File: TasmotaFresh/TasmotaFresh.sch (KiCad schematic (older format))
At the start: 0 parts

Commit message: initial schematic work
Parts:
- added D1, D2, D3: LED, symbol Device:LED
- added J1: ESP-01S, symbol Connector_Generic:Conn_02x04_Counter_Clockwise
- added J2: FAN, symbol Connector_Generic:Conn_01x04
- added Q1: HIGH, Package_TO_SOT_THT:TO-220-3_Vertical, symbol Triac_Thyristor:TIC226
- added Q2: MEDIUM, Package_TO_SOT_THT:TO-220-3_Vertical, symbol Triac_Thyristor:TIC226
- added Q3: LOW, Package_TO_SOT_THT:TO-220-3_Vertical, symbol Triac_Thyristor:TIC226
- added R1, R2, R3, R4: R, symbol Device:R
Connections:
- new net: J2.1 (Pin_1), Q1.1 (A1)
- new net: Q1.3 (G), R1.1
- new net: J2.2 (Pin_2), Q2.1 (A1)
- new net: Q2.3 (G), R2.1
- new net: J2.3 (Pin_3), Q3.1 (A1)
- new net: Q3.3 (G), R3.2
- new net: D1.1 (K), D2.1 (K), D3.1 (K), R4.1
- new net 3V3: J1.4 (Pin_4)
- new net CH_PD-EN: J1.2 (Pin_2)
- new net GND: J1.1 (Pin_1), J1.8 (Pin_8), R4.2
- new net GPIO0: D2.2 (A), J1.6 (Pin_6), R2.2
- new net GPIO2: D1.2 (A), J1.7 (Pin_7), R1.2
- new net GPIO3: D3.2 (A), J1.5 (Pin_5), R3.1
- new net LINE: Q1.2 (A2), Q2.2 (A2), Q3.2 (A2)
- new net NEUT: J2.4 (Pin_4)
- new net RST: J1.3 (Pin_3)

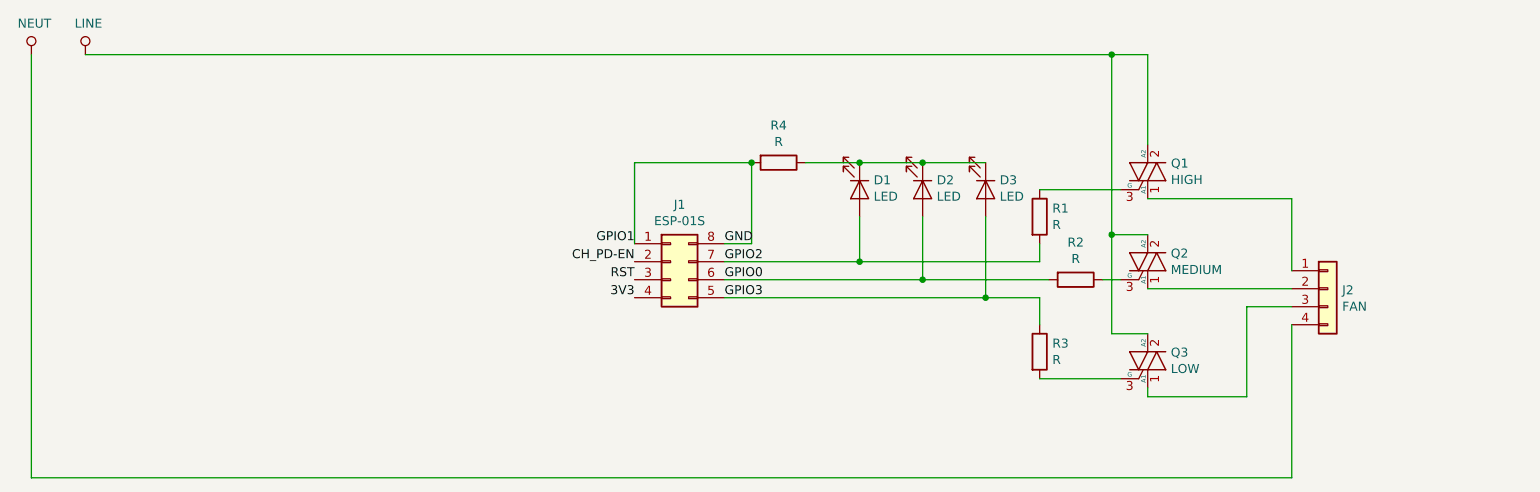
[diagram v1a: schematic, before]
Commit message: updated schematic with power supply section
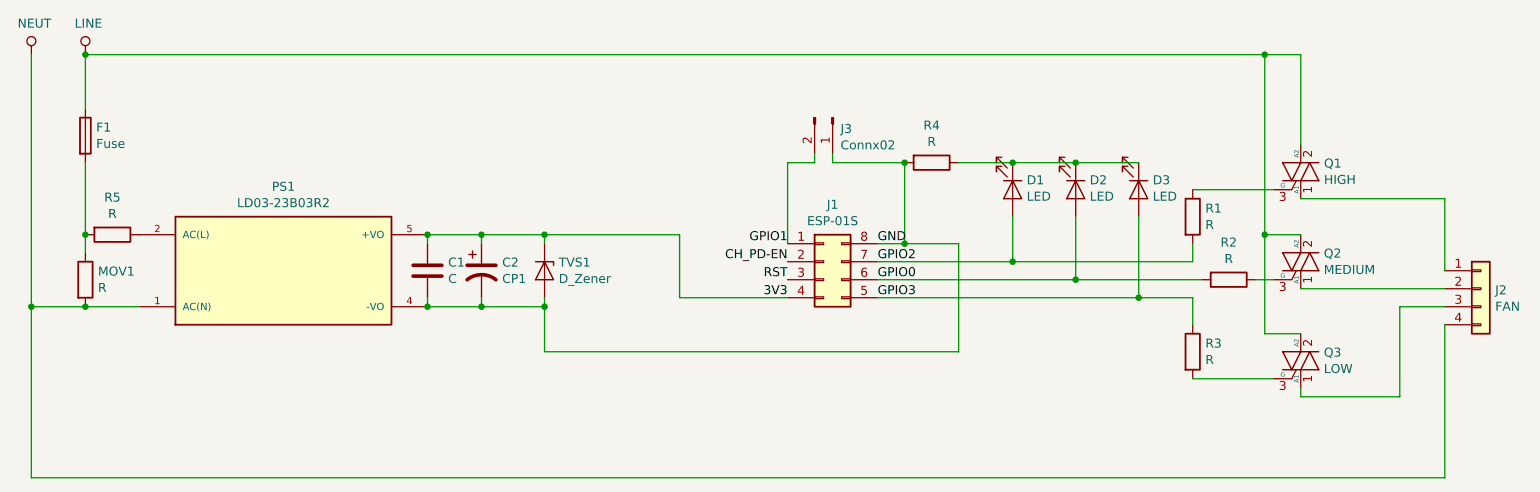
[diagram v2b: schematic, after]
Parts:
- added C1: C, symbol Device:C
- added C2: CP1, symbol Device:CP1
- added F1: Fuse, symbol Device:Fuse
- added J3: Connx02, symbol Connector:Conn_01x02_Male
- added MOV1, R5: R, symbol Device:R
- added PS1: LD03-23B03R2, CONV_LD03-23B03R2, symbol TasmotaFresh:LD03-23B03R2
- added TVS1: D_Zener, symbol Device:D_Zener
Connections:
- net 3V3: now also C1.1, C2.1, PS1.5 (+VO), TVS1.1 (K)
- net GND: now also C1.2, C2.2, J3.1 (Pin_1), PS1.4 (-VO), TVS1.2 (A); no longer J1.1 (Pin_1)
- net LINE: now also F1.1
- net NEUT: now also MOV1.2, PS1.1 (AC(N))
- new net: PS1.2 (AC(L)), R5.1
- new net: F1.2, MOV1.1, R5.2
- new net GPIO1: J1.1 (Pin_1), J3.2 (Pin_2)
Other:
- moved on the sheet: D1, D2, D3, J1, J2, Q1, Q2, Q3, R1, R2, R3, R4

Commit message: started using newer version of kicad, updated a few minor things
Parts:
- C1: symbol Device:C -> TasmotaFresh-rescue:C-Device
- C2: symbol Device:CP1 -> TasmotaFresh-rescue:CP1-Device
- D1, D2, D3: symbol Device:LED -> TasmotaFresh-rescue:LED-Device
- F1: symbol Device:Fuse -> TasmotaFresh-rescue:Fuse-Device
- J1: symbol Connector_Generic:Conn_02x04_Counter_Clockwise -> TasmotaFresh-rescue:Conn_02x04_Counter_Clockwise-Connector_Generic
- J2: symbol Connector_Generic:Conn_01x04 -> TasmotaFresh-rescue:Conn_01x04-Connector_Generic
- J3: symbol Connector:Conn_01x02_Male -> TasmotaFresh-rescue:Conn_01x02_Male-Connector
- MOV1, R1, R2, R3, R4, R5: symbol Device:R -> TasmotaFresh-rescue:R-Device
- PS1: footprint CONV_LD03-23B03R2 -> TasmotaFresh:CONV_LD03-23B03R2
- Q1, Q2, Q3: symbol Triac_Thyristor:TIC226 -> TasmotaFresh-rescue:TIC226-Triac_Thyristor
- TVS1: symbol Device:D_Zener -> TasmotaFresh-rescue:D_Zener-Device
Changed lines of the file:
@@
 $EndDescr
 $Comp
-L Connector_Generic:Conn_02x04_Counter_Clockwise J1
+L TasmotaFresh-rescue:Conn_02x04_Counter_Clockwise-Connector_Generic J1
 U 1 1 603C0E99
 P 5850 4350
@@
 GPIO3
 $Comp
-L Triac_Thyristor:TIC226 Q1
+L TasmotaFresh-rescue:TIC226-Triac_Thyristor Q1
 U 1 1 603C2944
 P 8500 3850
@@
 $EndComp
 $Comp
-L Triac_Thyristor:TIC226 Q2
+L TasmotaFresh-rescue:TIC226-Triac_Thyristor Q2
 U 1 1 603C3BA0
 P 8500 4350
@@
 $EndComp
 $Comp
-L Triac_Thyristor:TIC226 Q3
+L TasmotaFresh-rescue:TIC226-Triac_Thyristor Q3
 U 1 1 603C3F76
 P 8500 4900
@@
 	7900 5000 8350 5000
 $Comp
-L Device:R R1
+L TasmotaFresh-rescue:R-Device R1
 U 1 1 603CAB41
 P 7900 4100
@@
 $EndComp
 $Comp
-L Device:R R3
+L TasmotaFresh-rescue:R-Device R3
 U 1 1 603CB1AB
 P 7900 4850
@@
 $EndComp
 $Comp
-L Device:R R2
+L TasmotaFresh-rescue:R-Device R2
 U 1 1 603CB619
 P 8100 4450
@@
 	7900 4700 7900 4550
 $Comp
-L Connector_Generic:Conn_01x04 J2
+L TasmotaFresh-rescue:Conn_01x04-Connector_Generic J2
 U 1 1 603CCD5A
 P 9500 4500
@@
 	9050 4600 9300 4600
 $Comp
-L Device:LED D3
+L TasmotaFresh-rescue:LED-Device D3
 U 1 1 603DB2F3
 P 7600 3950
@@
 	7600 4100 7600 4550
 $Comp
-L Device:LED D2
+L TasmotaFresh-rescue:LED-Device D2
 U 1 1 603E0043
 P 7250 3950
@@
 	7250 3800 7600 3800
 $Comp
-L Device:LED D1
+L TasmotaFresh-rescue:LED-Device D1
 U 1 1 603E0C79
 P 6900 3950
@@
 	7250 4450 7950 4450
 $Comp
-L Device:R R4
+L TasmotaFresh-rescue:R-Device R4
 U 1 1 603EAC37
 P 6450 3800
@@
 	5650 4250 5650 3800
 $Comp
-L power:LINE #PWR?
+L TasmotaFresh-rescue:LINE-power #PWR0101
 U 1 1 60405C0C
 P 1750 3200
-F 0 "#PWR?" H 1750 3050 50  0001 C CNN
+F 0 "#PWR0101" H 1750 3050 50  0001 C CNN
 F 1 "LINE" H 1767 3373 50  0000 C CNN
 F 2 "" H 1750 3200 50  0001 C CNN
@@
 $EndComp
 $Comp
-L power:NEUT #PWR?
+L TasmotaFresh-rescue:NEUT-power #PWR0102
 U 1 1 60405F38
 P 1450 3200
-F 0 "#PWR?" H 1450 3050 50  0001 C CNN
+F 0 "#PWR0102" H 1450 3050 50  0001 C CNN
 F 1 "NEUT" H 1467 3373 50  0000 C CNN
 F 2 "" H 1450 3200 50  0001 C CNN
@@
 Connection ~ 8300 4200
 $Comp
-L Connector:Conn_01x02_Male J3
+L TasmotaFresh-rescue:Conn_01x02_Male-Connector J3
 U 1 1 608F8110
 P 5900 3550
@@
 F 0 "PS1" H 2850 4867 50  0000 C CNN
 F 1 "LD03-23B03R2" H 2850 4776 50  0000 C CNN
-F 2 "CONV_LD03-23B03R2" H 2650 4750 50  0001 L BNN
+F 2 "TasmotaFresh:CONV_LD03-23B03R2" H 2650 4750 50  0001 L BNN
 F 3 "" H 2650 4750 50  0001 L BNN
 	1    2850 4400
@@
 $EndComp
 $Comp
-L Device:R R5
+L TasmotaFresh-rescue:R-Device R5
 U 1 1 6090E65F
 P 1900 4200
@@
 $EndComp
 $Comp
-L Device:R MOV1
+L TasmotaFresh-rescue:R-Device MOV1
 U 1 1 6090F719
 P 1750 4450
@@
 $EndComp
 $Comp
-L Device:Fuse F1
+L TasmotaFresh-rescue:Fuse-Device F1
 U 1 1 6090FD5C
 P 1750 3650
@@
 	1750 3500 1750 3200
 $Comp
-L Device:C C1
+L TasmotaFresh-rescue:C-Device C1
 U 1 1 60914AAB
 P 3650 4400
@@
 $EndComp
 $Comp
-L Device:CP1 C2
+L TasmotaFresh-rescue:CP1-Device C2
 U 1 1 60915235
 P 3950 4400
@@
 $EndComp
 $Comp
-L Device:D_Zener TVS1
+L TasmotaFresh-rescue:D_Zener-Device TVS1
 U 1 1 60916FFB
 P 4300 4400

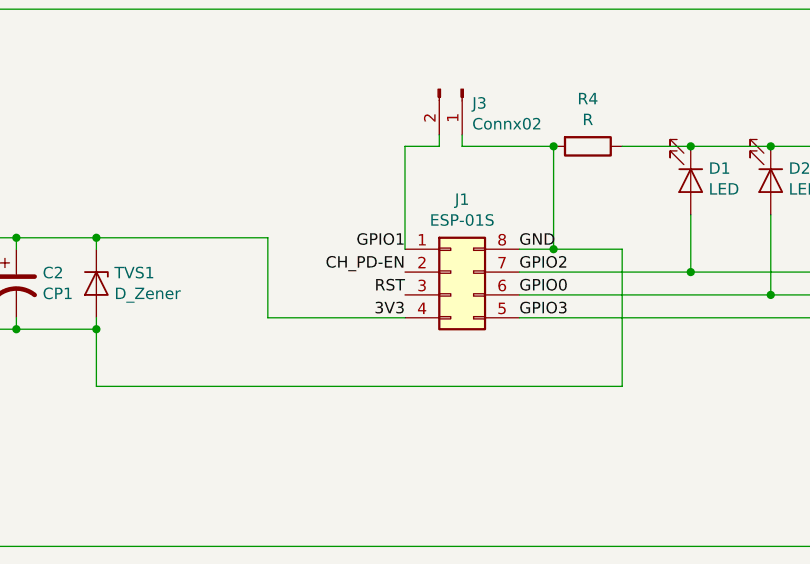
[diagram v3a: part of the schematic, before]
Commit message: correllaed footprints
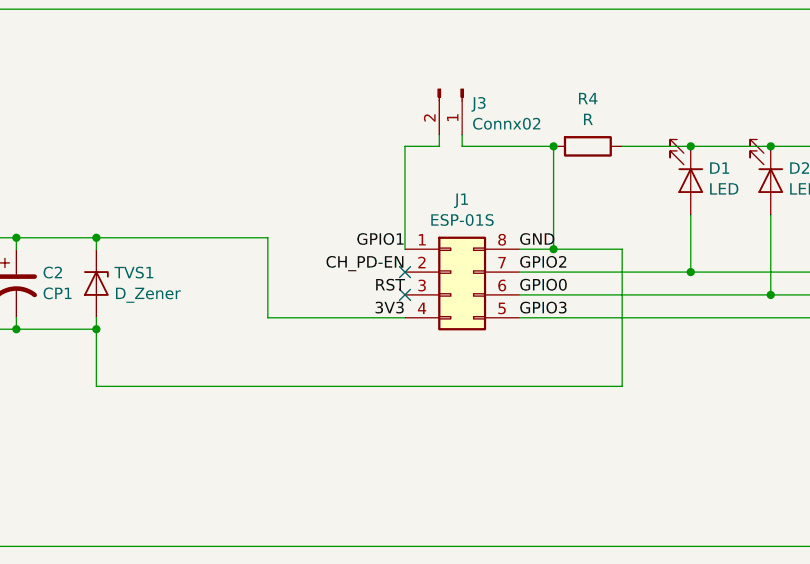
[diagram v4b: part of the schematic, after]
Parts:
- C1: footprint (none) -> Capacitors:CP_Radial_D5.0mm_P2.00mm
- C2: footprint (none) -> Capacitors:CP_Radial_D4.0mm_P2.00mm
- D1, D2, D3: footprint (none) -> LED:LED_D5.0mm
- F1: footprint (none) -> Fuse:Fuse_BelFuse_0ZRE0005FF_L8.3mm_W3.8mm
- J1: footprint (none) -> PinConn:PinHeader_2x04_P1.27mm_Vertical
- J2: footprint (none) -> Connectors:PinHeader_1x04_P2.00mm_Vertical
- J3: footprint (none) -> Connectors:PinHeader_1x02_P2.00mm_Vertical
- MOV1: footprint (none) -> Resistors:R_Radial_Power_L11.0mm_W7.0mm_P5.00mm
- Q1, Q2, Q3: footprint Package_TO_SOT_THT:TO-220-3_Vertical -> Transistor:TO-220-3_Vertical
- R1, R2, R3, R4: footprint (none) -> Resistors:R_Axial_DIN0204_L3.6mm_D1.6mm_P7.62mm_Horizontal
- R5: footprint (none) -> Resistors:R_Axial_Power_L20.0mm_W6.4mm_P22.40mm
- TVS1: footprint (none) -> Diodes:D_A-405_P7.62mm_Horizontal
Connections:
- no-connect marks 0 -> 2
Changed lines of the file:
@@
 F 0 "J1" H 5900 4667 50  0000 C CNN
 F 1 "ESP-01S" H 5900 4576 50  0000 C CNN
-F 2 "" H 5850 4350 50  0001 C CNN
+F 2 "PinConn:PinHeader_2x04_P1.27mm_Vertical" H 5850 4350 50  0001 C CNN
 F 3 "~" H 5850 4350 50  0001 C CNN
 	1    5850 4350
@@
 F 0 "Q1" H 8629 3896 50  0000 L CNN
 F 1 "HIGH" H 8629 3805 50  0000 L CNN
-F 2 "Package_TO_SOT_THT:TO-220-3_Vertical" H 8700 3775 50  0001 L CIN
+F 2 "Transistor:TO-220-3_Vertical" H 8700 3775 50  0001 L CIN
 F 3 "http://pdf.datasheetcatalog.com/datasheet/PowerInnovations/mXuqxvy.pdf" H 8500 3850 50  0001 L CNN
 	1    8500 3850
@@
 F 0 "Q2" H 8628 4396 50  0000 L CNN
 F 1 "MEDIUM" H 8628 4305 50  0000 L CNN
-F 2 "Package_TO_SOT_THT:TO-220-3_Vertical" H 8700 4275 50  0001 L CIN
+F 2 "Transistor:TO-220-3_Vertical" H 8700 4275 50  0001 L CIN
 F 3 "http://pdf.datasheetcatalog.com/datasheet/PowerInnovations/mXuqxvy.pdf" H 8500 4350 50  0001 L CNN
 	1    8500 4350
@@
 F 0 "Q3" H 8628 4946 50  0000 L CNN
 F 1 "LOW" H 8628 4855 50  0000 L CNN
-F 2 "Package_TO_SOT_THT:TO-220-3_Vertical" H 8700 4825 50  0001 L CIN
+F 2 "Transistor:TO-220-3_Vertical" H 8700 4825 50  0001 L CIN
 F 3 "http://pdf.datasheetcatalog.com/datasheet/PowerInnovations/mXuqxvy.pdf" H 8500 4900 50  0001 L CNN
 	1    8500 4900
@@
 F 0 "R1" H 7970 4146 50  0000 L CNN
 F 1 "R" H 7970 4055 50  0000 L CNN
-F 2 "" V 7830 4100 50  0001 C CNN
+F 2 "Resistors:R_Axial_DIN0204_L3.6mm_D1.6mm_P7.62mm_Horizontal" V 7830 4100 50  0001 C CNN
 F 3 "~" H 7900 4100 50  0001 C CNN
 	1    7900 4100
@@
 F 0 "R3" H 7970 4896 50  0000 L CNN
 F 1 "R" H 7970 4805 50  0000 L CNN
-F 2 "" V 7830 4850 50  0001 C CNN
+F 2 "Resistors:R_Axial_DIN0204_L3.6mm_D1.6mm_P7.62mm_Horizontal" V 7830 4850 50  0001 C CNN
 F 3 "~" H 7900 4850 50  0001 C CNN
 	1    7900 4850
@@
 F 0 "R2" V 7893 4450 50  0000 C CNN
 F 1 "R" V 7984 4450 50  0000 C CNN
-F 2 "" V 8030 4450 50  0001 C CNN
+F 2 "Resistors:R_Axial_DIN0204_L3.6mm_D1.6mm_P7.62mm_Horizontal" V 8030 4450 50  0001 C CNN
 F 3 "~" H 8100 4450 50  0001 C CNN
 	1    8100 4450
@@
 F 0 "J2" H 9580 4492 50  0000 L CNN
 F 1 "FAN" H 9580 4401 50  0000 L CNN
-F 2 "" H 9500 4500 50  0001 C CNN
+F 2 "Connectors:PinHeader_1x04_P2.00mm_Vertical" H 9500 4500 50  0001 C CNN
 F 3 "~" H 9500 4500 50  0001 C CNN
 	1    9500 4500
@@
 F 0 "D3" V 7547 4028 50  0000 L CNN
 F 1 "LED" V 7638 4028 50  0000 L CNN
-F 2 "" H 7600 3950 50  0001 C CNN
+F 2 "LED:LED_D5.0mm" H 7600 3950 50  0001 C CNN
 F 3 "~" H 7600 3950 50  0001 C CNN
 	1    7600 3950
@@
 F 0 "D2" V 7197 4028 50  0000 L CNN
 F 1 "LED" V 7288 4028 50  0000 L CNN
-F 2 "" H 7250 3950 50  0001 C CNN
+F 2 "LED:LED_D5.0mm" H 7250 3950 50  0001 C CNN
 F 3 "~" H 7250 3950 50  0001 C CNN
 	1    7250 3950
@@
 F 0 "D1" V 6847 4028 50  0000 L CNN
 F 1 "LED" V 6938 4028 50  0000 L CNN
-F 2 "" H 6900 3950 50  0001 C CNN
+F 2 "LED:LED_D5.0mm" H 6900 3950 50  0001 C CNN
 F 3 "~" H 6900 3950 50  0001 C CNN
 	1    6900 3950
@@
 F 0 "R4" V 6243 3800 50  0000 C CNN
 F 1 "R" V 6334 3800 50  0000 C CNN
-F 2 "" V 6380 3800 50  0001 C CNN
+F 2 "Resistors:R_Axial_DIN0204_L3.6mm_D1.6mm_P7.62mm_Horizontal" V 6380 3800 50  0001 C CNN
 F 3 "~" H 6450 3800 50  0001 C CNN
 	1    6450 3800
@@
 F 0 "J3" V 5962 3594 50  0000 L CNN
 F 1 "Connx02" V 6053 3594 50  0000 L CNN
-F 2 "" H 5900 3550 50  0001 C CNN
+F 2 "Connectors:PinHeader_1x02_P2.00mm_Vertical" H 5900 3550 50  0001 C CNN
 F 3 "~" H 5900 3550 50  0001 C CNN
 	1    5900 3550
@@
 F 0 "R5" V 1693 4200 50  0000 C CNN
 F 1 "R" V 1784 4200 50  0000 C CNN
-F 2 "" V 1830 4200 50  0001 C CNN
+F 2 "Resistors:R_Axial_Power_L20.0mm_W6.4mm_P22.40mm" V 1830 4200 50  0001 C CNN
 F 3 "~" H 1900 4200 50  0001 C CNN
 	1    1900 4200
@@
 F 0 "MOV1" H 1820 4496 50  0000 L CNN
 F 1 "R" H 1820 4405 50  0000 L CNN
-F 2 "" V 1680 4450 50  0001 C CNN
+F 2 "Resistors:R_Radial_Power_L11.0mm_W7.0mm_P5.00mm" V 1680 4450 50  0001 C CNN
 F 3 "~" H 1750 4450 50  0001 C CNN
 	1    1750 4450
@@
 F 0 "F1" H 1810 3696 50  0000 L CNN
 F 1 "Fuse" H 1810 3605 50  0000 L CNN
-F 2 "" V 1680 3650 50  0001 C CNN
+F 2 "Fuse:Fuse_BelFuse_0ZRE0005FF_L8.3mm_W3.8mm" V 1680 3650 50  0001 C CNN
 F 3 "~" H 1750 3650 50  0001 C CNN
 	1    1750 3650
@@
 F 0 "C1" H 3765 4446 50  0000 L CNN
 F 1 "C" H 3765 4355 50  0000 L CNN
-F 2 "" H 3688 4250 50  0001 C CNN
+F 2 "Capacitors:CP_Radial_D5.0mm_P2.00mm" H 3688 4250 50  0001 C CNN
 F 3 "~" H 3650 4400 50  0001 C CNN
 	1    3650 4400
@@
 F 0 "C2" H 4065 4446 50  0000 L CNN
 F 1 "CP1" H 4065 4355 50  0000 L CNN
-F 2 "" H 3950 4400 50  0001 C CNN
+F 2 "Capacitors:CP_Radial_D4.0mm_P2.00mm" H 3950 4400 50  0001 C CNN
 F 3 "~" H 3950 4400 50  0001 C CNN
 	1    3950 4400
@@
 F 0 "TVS1" V 4254 4479 50  0000 L CNN
 F 1 "D_Zener" V 4345 4479 50  0000 L CNN
-F 2 "" H 4300 4400 50  0001 C CNN
+F 2 "Diodes:D_A-405_P7.62mm_Horizontal" H 4300 4400 50  0001 C CNN
 F 3 "~" H 4300 4400 50  0001 C CNN
 	1    4300 4400
@@
 Connection ~ 4300 4600
 Connection ~ 6300 4250
+NoConn ~ 5650 4450
+NoConn ~ 5650 4350
 $EndSCHEMATC
